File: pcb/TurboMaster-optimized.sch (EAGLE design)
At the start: 40 parts, among them IC1 74LS244N, IC10 74LS32N, IC11 74LS244N, IC12 PAL16L8, IC13 PAL16L8, IC14 PAL16R4, IC15 PAL16R6, IC16 62256, IC17 62256, IC19 65C02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

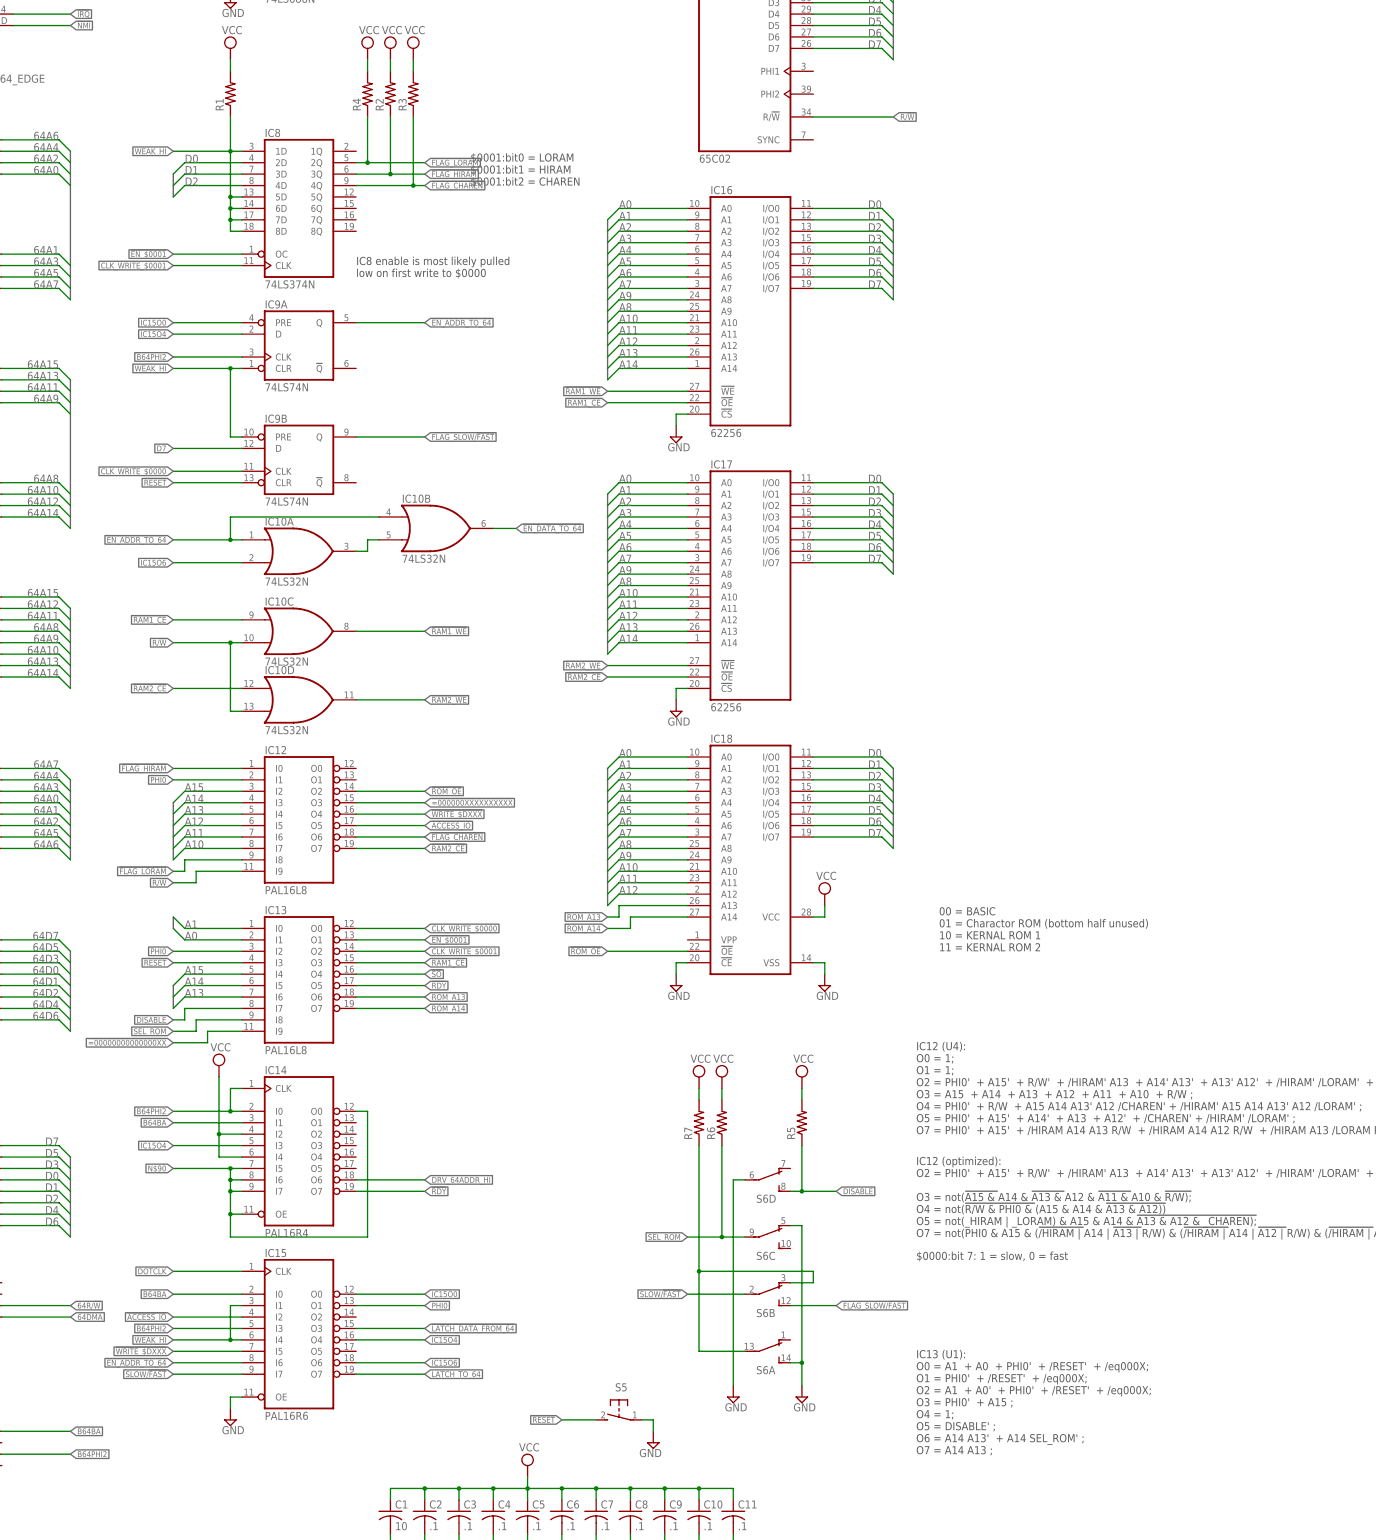
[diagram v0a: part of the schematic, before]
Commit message: Schematic signal naming updates
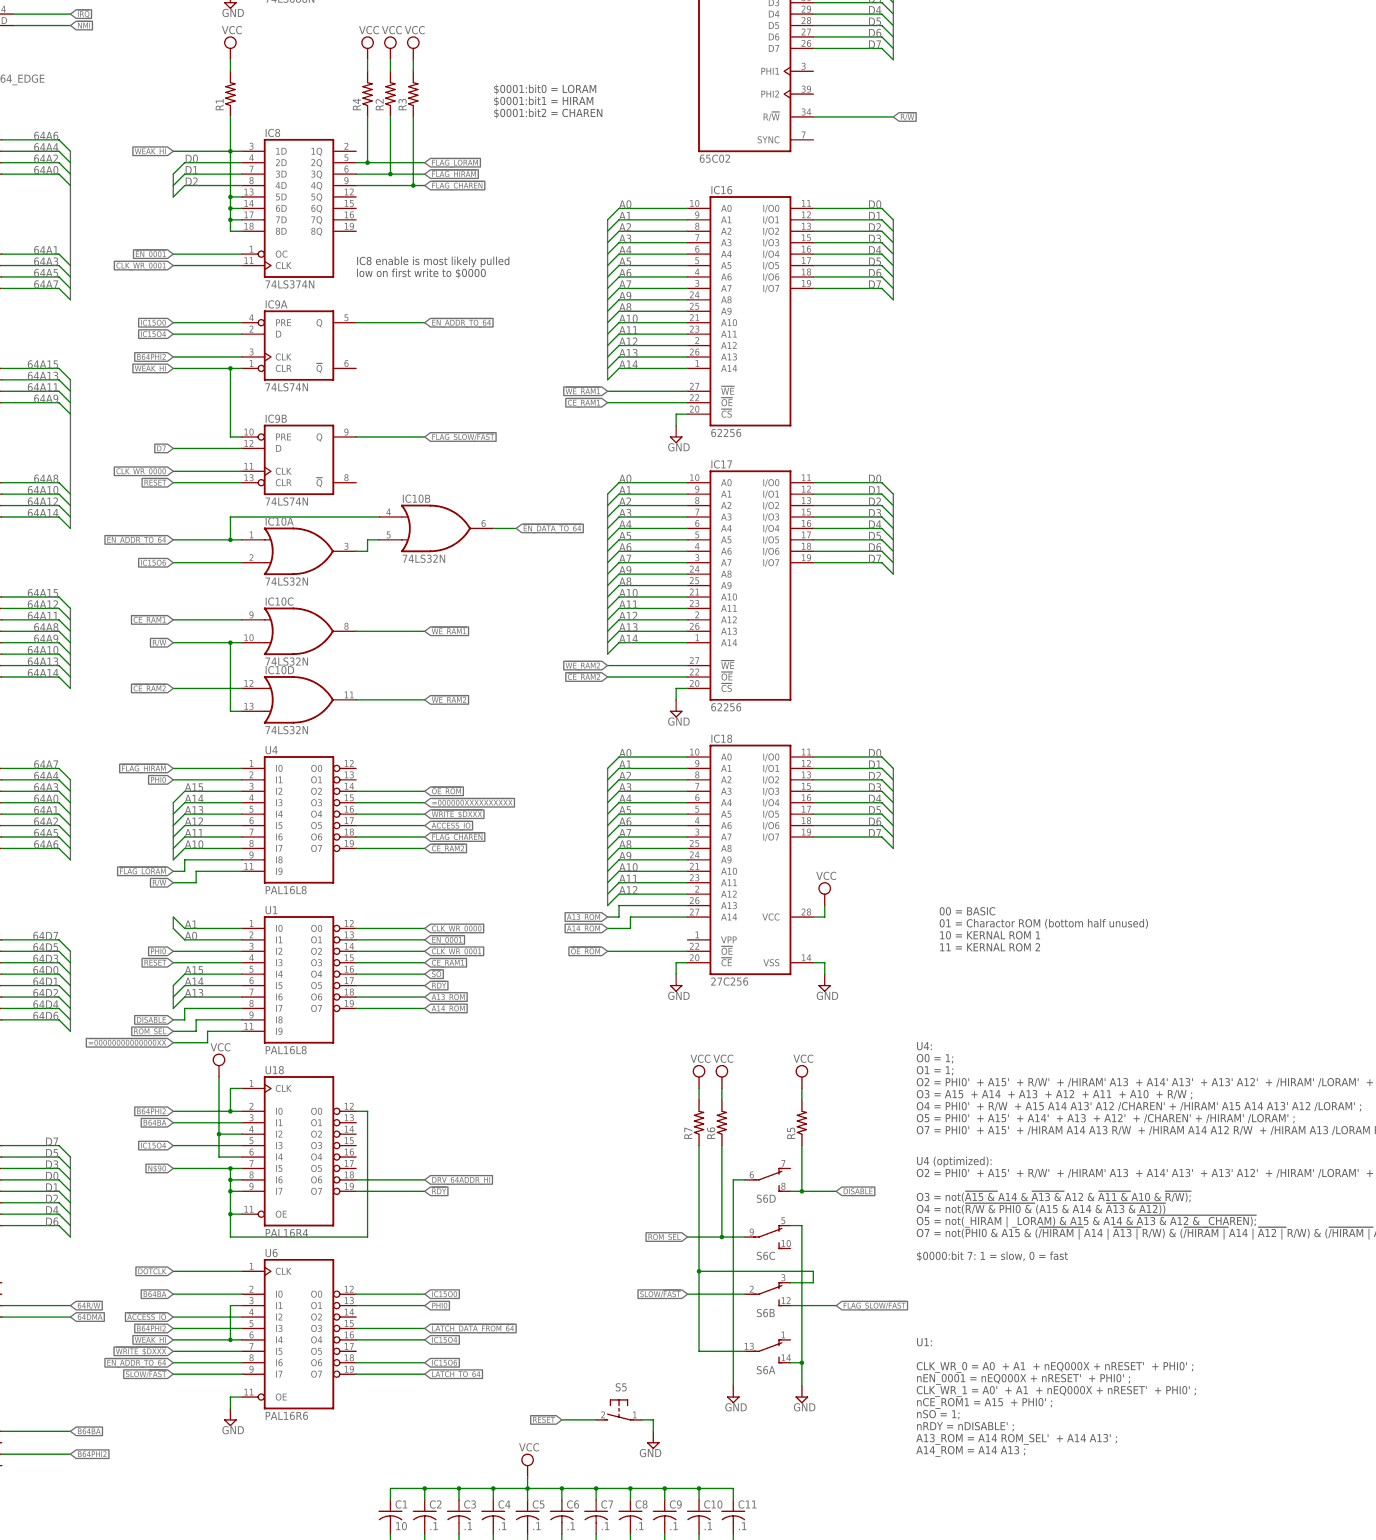
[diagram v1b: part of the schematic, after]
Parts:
- IC18: value (none) -> 27C256
- renumbered IC12 to U4, IC13 to U1, IC14 to U18, IC15 to U6
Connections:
- net !EN_$0001 renamed !EN_0001
- net !RAM1_CE renamed !CE_RAM1
- net !RAM1_WE renamed !WE_RAM1
- net !RAM2_CE renamed !CE_RAM2
- net !RAM2_WE renamed !WE_RAM2
- net !ROM_OE renamed !OE_ROM
- net CLK_WRITE_$0000 renamed CLK_WR_0000
- net CLK_WRITE_$0001 renamed CLK_WR_0001
- net ROM_A13 renamed A13_ROM
- net ROM_A14 renamed A14_ROM
- net SEL_ROM renamed ROM_SEL
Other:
- note added: "U1: CLK_WR_0 = A0 + A1 + nEQ000X + nRESET' + PHI0' ; nEN_0001 = nEQ000X + nRESET' + PHI0' ; CLK_WR_1 = A0' + A1 + nEQ000X + nRESET' + PHI0' ; nCE_ROM1 = A15 + PHI0' ; nSO = 1; nRDY = nDISABLE' ; A13_ROM = A14 ROM_SEL' + A14 A13' ; A14_ROM = A14 A13 ;"
- note added: "U4 (optimized): O2 = PHI0' + A15' + R/W' + /HIRAM' A13 + A14' A13' + A13' A12' + /HIRAM' /LORAM' + A14' /LORAM' + A13' /CHAREN; O3 = not(!A15 & !A14 & !A13 & !A12 & !A11 & !A10 & !R/W); O4 = not(!R/W & PHI0 & !(A15 & A14 & !A13 & A12)) O5 = not(_HIRAM | _LORAM) & A15 & A14 & !A13 & A12 & _CHAREN); O7 = not(PHI0 & A15 & (!/HIRAM | !A14 | !A13 | !R/W) & (!/HIRAM | !A14 | !A12 | !R/W) & (!/HIRAM | !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"
- note added: "U4: O0 = 1; O1 = 1; O2 = PHI0' + A15' + R/W' + /HIRAM' A13 + A14' A13' + A13' A12' + /HIRAM' /LORAM' + A14' /LORAM' + A13' /CHAREN; O3 = A15 + A14 + A13 + A12 + A11 + A10 + R/W ; O4 = PHI0' + R/W + A15 A14 A13' A12 /CHAREN' + /HIRAM' A15 A14 A13' A12 /LORAM' ; O5 = PHI0' + A15' + A14' + A13 + A12' + /CHAREN' + /HIRAM' /LORAM' ; O7 = PHI0' + A15' + /HIRAM A14 A13 R/W + /HIRAM A14 A12 R/W + /HIRAM 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"
- note removed: "IC12 (U4): O0 = 1; O1 = 1; O2 = PHI0' + A15' + R/W' + /HIRAM' A13 + A14' A13' + A13' A12' + /HIRAM' /LORAM' + A14' /LORAM' + A13' /CHAREN; O3 = A15 + A14 + A13 + A12 + A11 + A10 + R/W ; O4 = PHI0' + R/W + A15 A14 A13' A12 /CHAREN' + /HIRAM' A15 A14 A13' A12 /LORAM' ; O5 = PHI0' + A15' + A14' + A13 + A12' + /CHAREN' + /HIRAM' /LORAM' ; O7 = PHI0' + A15' + /HIRAM A14 A13 R/W + /HIRAM A14 A12 R/W + 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"
- note removed: "IC12 (optimized): O2 = PHI0' + A15' + R/W' + /HIRAM' A13 + A14' A13' + A13' A12' + /HIRAM' /LORAM' + A14' /LORAM' + A13' /CHAREN; O3 = not(!A15 & !A14 & !A13 & !A12 & !A11 & !A10 & !R/W); O4 = not(!R/W & PHI0 & !(A15 & A14 & !A13 & A12)) O5 = not(_HIRAM | _LORAM) & A15 & A14 & !A13 & A12 & _CHAREN); O7 = not(PHI0 & A15 & (!/HIRAM | !A14 | !A13 | !R/W) & (!/HIRAM | !A14 | !A12 | !R/W) & (!/HIRAM |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"
- note removed: "IC13 (U1): O0 = A1 + A0 + PHI0' + /RESET' + /eq000X; O1 = PHI0' + /RESET' + /eq000X; O2 = A1 + A0' + PHI0' + /RESET' + /eq000X; O3 = PHI0' + A15 ; O4 = 1; O5 = DISABLE' ; O6 = A14 A13' + A14 SEL_ROM' ; O7 = A14 A13 ;"
